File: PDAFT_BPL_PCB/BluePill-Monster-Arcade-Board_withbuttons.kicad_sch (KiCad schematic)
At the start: 19 parts, among them J1 Conn_01x02, J2 Conn_01x04, U1 YAAJ_BluePill_Part_Like, U2 ProMicro, U3 ULN2003, U4 ULN2003

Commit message: bluepill update
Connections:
- net at Arduino_power1.1 (Pin_1), Circle1.1 (Pin_1), Cross1.1 (Pin_1)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: now also U2.21 (VCC); no longer J1.1 (Pin_1), J2.1 (Pin_1), U1.18 (5V)
- net at Arduino_power1.2 (Pin_2): now also J1.1 (Pin_1), J2.1 (Pin_1), U1.18 (5V); no longer U2.21 (VCC)
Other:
- moved on the sheet: Arduino_power1
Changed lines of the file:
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@@
   (junction (at 258.7571 84.6513) (diameter 1.016) (color 0 0 0 0))
   (junction (at 258.7571 96.2315) (diameter 1.016) (color 0 0 0 0))
-  (wire (pts (xy -4.6314 104.3374) (xy -4.472 48.7213))
-    (stroke (width 0) (type solid) (color 0 0 0 0))
-  )
   (wire (pts (xy -4.472 48.7213) (xy 115.6889 48.7213))
     (stroke (width 0) (type solid) (color 0 0 0 0))
   )
+  (wire (pts (xy -3.8711 63.7968) (xy -4.472 48.7213))
+    (stroke (width 0) (type solid) (color 0 0 0 0))
+  )
+  (wire (pts (xy -3.8711 66.3368) (xy -4.6314 104.3374))
+    (stroke (width 0) (type solid) (color 0 0 0 0))
+  )
   (wire (pts (xy 7.225 91.1846) (xy 7.2844 90.4432))
     (stroke (width 0) (type solid) (color 0 0 0 0))
@@
     (stroke (width 0) (type solid) (color 0 0 0 0))
   )
-  (wire (pts (xy 219.0154 62.8944) (xy 219.0154 79.1587))
+  (wire (pts (xy 219.0154 60.3544) (xy 219.0154 79.1587))
     (stroke (width 0) (type solid) (color 0 0 0 0))
   )
@@
   (wire (pts (xy 260.5499 96.2315) (xy 258.7571 96.2315))
     (stroke (width 0) (type solid) (color 0 0 0 0))
+  )
+  (symbol (lib_id "Connector_Generic:Conn_01x02") (at 1.2089 63.7968 0) (unit 1)
+    (in_bom yes) (on_board yes) (fields_autoplaced)
+    (property "Reference" "Arduino_power1" (id 0) (at 3.241 64.1583 0)
+      (effects (font (size 1.27 1.27)) (justify left))
+    )
+    (property "Value" "Conn_01x02" (id 1) (at 3.241 66.9334 0)
+      (effects (font (size 1.27 1.27)) (justify left))
+    )
+    (property "Footprint" "Connector_JST:JST_XH_B2B-XH-A_1x02_P2.50mm_Vertical" (id 2) (at 1.2089 63.7968 0)
+      (effects (font (size 1.27 1.27)) hide)
+    )
+    (property "Datasheet" "~" (id 3) (at 1.2089 63.7968 0)
+      (effects (font (size 1.27 1.27)) hide)
+    )
+    (pin "1")
+    (pin "2")
   )
   (symbol (lib_id "Connector_Generic:Conn_01x02") (at 7.2844 85.3632 90) (unit 1)
@@
       (effects (font (size 1.27 1.27)) hide)
     )
-    (pin "1")
-    (pin "2")
-  )
-  (symbol (lib_id "Connector_Generic:Conn_01x02") (at 224.0954 60.3544 0) (unit 1)
-    (in_bom yes) (on_board yes) (fields_autoplaced)
-    (property "Reference" "Arduino_power1" (id 0) (at 226.1275 60.7159 0)
-      (effects (font (size 1.27 1.27)) (justify left))
-    )
-    (property "Value" "Conn_01x02" (id 1) (at 226.1275 63.491 0)
-      (effects (font (size 1.27 1.27)) (justify left))
-    )
-    (property "Footprint" "Connector_JST:JST_XH_B2B-XH-A_1x02_P2.50mm_Vertical" (id 2) (at 224.0954 60.3544 0)
-      (effects (font (size 1.27 1.27)) hide)
-    )
-    (property "Datasheet" "~" (id 3) (at 224.0954 60.3544 0)
-      (effects (font (size 1.27 1.27)) hide)
-    )

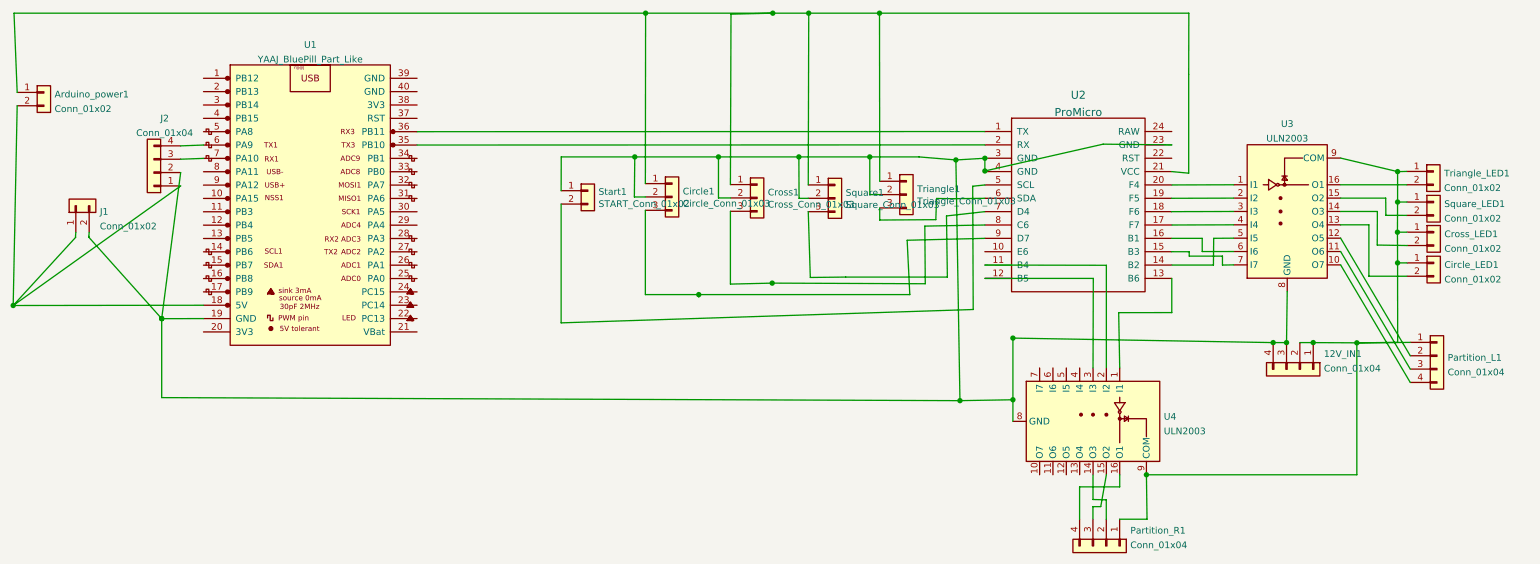
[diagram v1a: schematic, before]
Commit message: Update of bluepill moster with buttons to order on JLCPCB
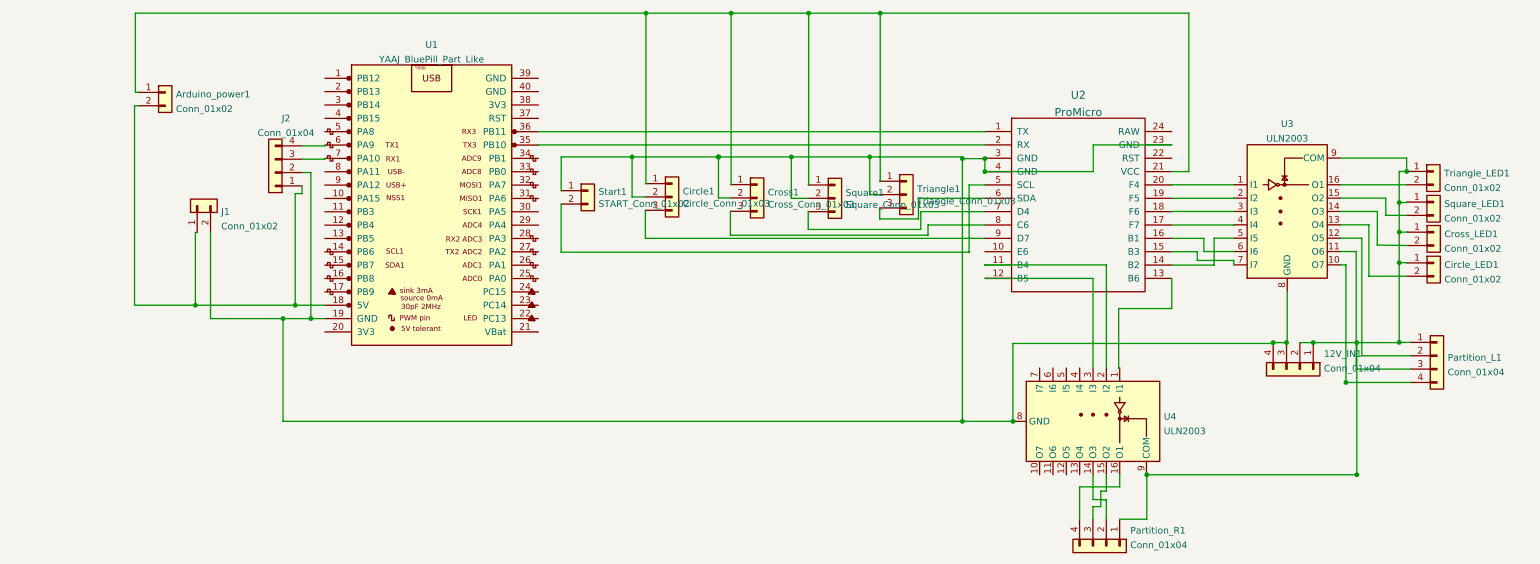
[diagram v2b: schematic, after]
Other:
- moved on the sheet: Arduino_power1, J1, J2, U1
